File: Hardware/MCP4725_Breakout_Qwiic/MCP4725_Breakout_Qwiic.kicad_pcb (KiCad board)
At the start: 2 copper layers, 25.4 x 25.4 mm, 49 parts, among them J1 Conn_01x02, J2 I2C, J3 Qwiic_RA, J4 Qwiic_RA, U2 MCP4725

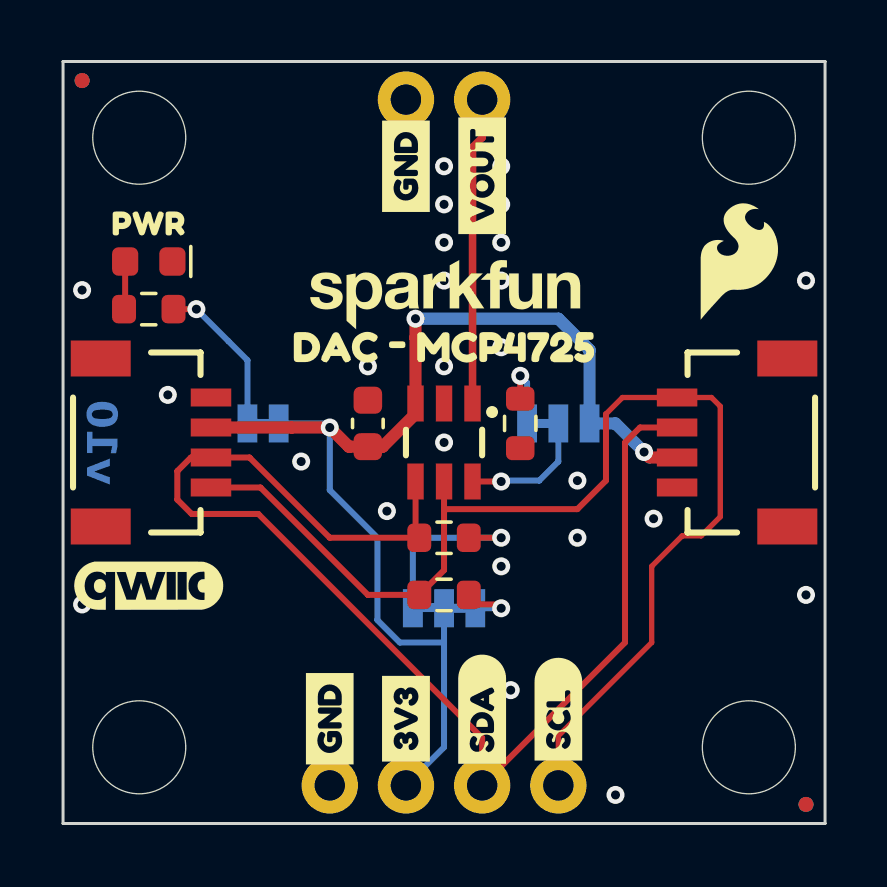
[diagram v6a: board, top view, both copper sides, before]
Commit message: Changes dual to single jumper
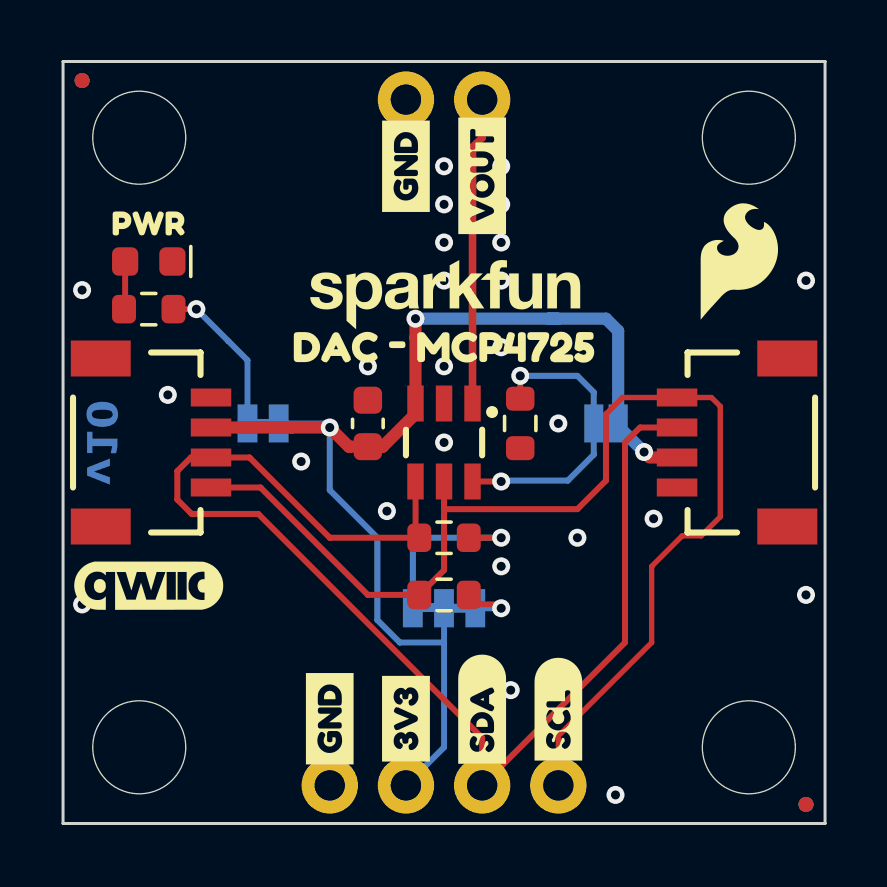
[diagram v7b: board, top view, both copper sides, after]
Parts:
- removed the G*** at (149.5, 91.4)
- removed the G*** at (153.7, 94.0)
- added G***: LOGO, SparkFun-Aesthetic:SparkFun_Logo_9mm, B.Cu at (153.7, 95.2)
- added kibuzzard-69BC563E: G***, kibuzzard-69BC563E, B.Cu at (162.9, 101.9)
- added kibuzzard-69BC5645: G***, kibuzzard-69BC5645, B.Cu at (163.2, 103.2)
- JP2: footprint SparkFun-Jumper:Jumper_3_NC-1_Trace -> SparkFun-Jumper:Jumper_2_NO
- moved kibuzzard-69B97714 6.55 mm to (159.4, 103.2)
- moved kibuzzard-69B9770D 3.13 mm to (159.4, 101.9)
- moved JP2 1.59 mm to (159.1, 99.1)
- moved kibuzzard-69BC0559 1.59 mm to (159.1, 100.7)
- moved kibuzzard-69BC0544 1.08 mm to (153.5, 96.8)
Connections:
- JP2 pad 1: Net-(JP2-A) -> ADDR
- JP2 pad 2: ADDR -> 3.3V
- R1 pad 2: Net-(JP2-A) -> ADDR
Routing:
- net ADDR: track 4.41 -> 9.93 mm, vias 1 -> 2
- net Net-(JP2-A): track 2.44 -> 0.00 mm, vias 1 -> 0
- net 3.3V: track 40.6 -> 41.1 mm

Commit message: Fixes jumpers on more time
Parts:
- JP2: footprint SparkFun-Jumper:Jumper_2_NO -> SparkFun-Jumper:Jumper_2_NC_Trace
- moved kibuzzard-69BC563E 1.42 mm to (162.2, 103.2)
- moved kibuzzard-69BC5645 1.37 mm to (162.7, 101.9)
- moved JP2 0.63 mm to (158.4, 99.1)
- moved kibuzzard-69B9770D 0.63 mm to (158.8, 101.9)
- moved kibuzzard-69B97714 0.63 mm to (158.8, 103.2)
- moved kibuzzard-69BC0559 0.63 mm to (158.4, 100.7)
- moved kibuzzard-69BC0561 0.32 mm to (148.0, 100.6)
- moved JP3 0.32 mm to (148.0, 99.1)
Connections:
- JP2 pad 1: ADDR -> GND
- JP2 pad 2: 3.3V -> ADDR
- R1 pad 1: GND -> ADDR
- R1 pad 2: ADDR -> 3.3V
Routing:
- net ADDR: track 9.93 -> 6.84 mm, vias 2 -> 1
- net 3.3V: track 41.1 -> 43.4 mm, vias 3 -> 4
